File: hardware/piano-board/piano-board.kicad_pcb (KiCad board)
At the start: 2 copper layers, 100 x 60 mm, 29 parts, among them J1 AVR-ISP-6, Q1 Q_NMOS_GSD, Q2 Q_PMOS_GSD, SW1 SW_SPDT, U1 ATmega328PB-A

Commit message: Improve CR2032 holder footprint
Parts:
- moved BT1 3.05 mm to (238.2, 51.8), turned to -45 degrees
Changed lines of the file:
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@@
 	(footprint "Thanassis_Foot:MP000360"
 		(layer "F.Cu")
-		(at 236.5 49.25)
+		(at 238.25 51.75 -45)
 		(property "Reference" "BT1"
-			(at 0 3.75 0)
+			(at 0 3.749999 -45)
 			(unlocked yes)
 			(layer "F.SilkS")
@@
 		)
 		(property "Value" "Battery_Cell"
-			(at 0 1 0)
+			(at 0 1 -45)
 			(unlocked yes)
 			(layer "F.Fab")
@@
 		)
 		(property "Footprint" "Thanassis_Foot:MP000360"
-			(at 0 0 0)
+			(at 0 0 -45)
 			(unlocked yes)
 			(layer "F.Fab")
@@
 		)
 		(property "Datasheet" ""
-			(at 0 0 0)
+			(at 0 0 -45)
 			(unlocked yes)
 			(layer "F.Fab")
@@
 		)
 		(property "Description" "Single-cell battery"
-			(at 0 0 0)
+			(at 0 0 -45)
 			(unlocked yes)
 			(layer "F.Fab")
@@
 		(attr through_hole)
 		(fp_line
-			(start -10.6 -5)
-			(end -10.6 5)
-			(stroke
-				(width 0.12)
-				(type default)
-			)
-			(layer "F.SilkS")
-		)
-		(fp_line
 			(start -10.6 5)
 			(end -3.9 10.25)
@@
 		)
 		(fp_line
+			(start -10.6 5)
+			(end -10.6 2.5)
+			(stroke
+				(width 0.12)
+				(type default)
+			)
+			(layer "F.SilkS")
+		)
+		(fp_line
 			(start -3.9 10.25)
 			(end 3.9 10.25)
@@
 		)
 		(fp_line
+			(start -10.6 -5)
+			(end -10.6 -2.5)
+			(stroke
+				(width 0.12)
+				(type default)
+			)
+			(layer "F.SilkS")
+		)
+		(fp_line
+			(start -6.51 -7.99)
+			(end -10.6 -5)
+			(stroke
+				(width 0.12)
+				(type default)
+			)
+			(layer "F.SilkS")
+		)
+		(fp_line
+			(start -6.51 -7.99)
+			(end -4 -7.99)
+			(stroke
+				(width 0.12)
+				(type default)
+			)
+			(layer "F.SilkS")
+		)
+		(fp_line
+			(start 10.6 2.5)
+			(end 10.6 5)
+			(stroke
+				(width 0.12)
+				(type default)
+			)
+			(layer "F.SilkS")
+		)
+		(fp_line
+			(start 4 -7.99)
+			(end 6.51 -7.99)
+			(stroke
+				(width 0.12)
+				(type default)
+			)
+			(layer "F.SilkS")
+		)
+		(fp_line
+			(start 6.51 -7.99)
+			(end 10.6 -5)
+			(stroke
+				(width 0.12)
+				(type default)
+			)
+			(layer "F.SilkS")
+		)
+		(fp_line
 			(start 10.6 -5)
-			(end 10.6 5)
-			(stroke
-				(width 0.12)
-				(type default)
-			)
-			(layer "F.SilkS")
-		)
-		(fp_line
-			(start -10.6 -7.99)
-			(end 10.6 -7.99)
-			(stroke
-				(width 0.12)
-				(type default)
-			)
+			(end 10.6 -2.5)
+			(stroke
+				(width 0.12)
+				(type default)
+			)
+			(layer "F.SilkS")
+		)
+		(fp_arc
+			(start 4 -7.99)
+			(mid 0 -6.737326)
+			(end -4 -7.99)
+			(stroke
+				(width 0.12)
+				(type default)
+			)
+			(layer "F.SilkS")
+		)
+		(fp_circle
+			(center 0 0)
+			(end 10 0)
+			(stroke
+				(width 0.12)
+				(type dash)
+			)
+			(fill none)
 			(layer "Dwgs.User")
-		)
-		(fp_line
-			(start -13 -8.5)
-			(end -13 5)
-			(stroke
-				(width 0.05)
-				(type default)
-			)
-			(layer "F.CrtYd")
 		)
 		(fp_line
@@
 		)
 		(fp_line
+			(start -13 -5)
+			(end -13 5)
+			(stroke
+				(width 0.05)
+				(type default)
+			)
+			(layer "F.CrtYd")
+		)
+		(fp_line
 			(start 4.000001 11)
 			(end 13 5)
@@
 		)
 		(fp_line
-			(start 13 -8.5)
-			(end -13 -8.5)
+			(start -5.5 -10.5)
+			(end -13 -5)
 			(stroke
 				(width 0.05)
@@
 		(fp_line
 			(start 13 5)
-			(end 13 -8.5)
+			(end 13 -5)
+			(stroke
+				(width 0.05)
+				(type default)
+			)
+			(layer "F.CrtYd")
+		)
+		(fp_line
+			(start 5.5 -10.5)
+			(end -5.5 -10.5)
+			(stroke
+				(width 0.05)
+				(type default)
+			)
+			(layer "F.CrtYd")
+		)
+		(fp_line
+			(start 13 -5)
+			(end 5.5 -10.5)
 			(stroke
 				(width 0.05)
@@
 		)
 		(fp_text user "+"
-			(at 0 7.5 0)
+			(at 0 7.5 -45)
 			(unlocked yes)
 			(layer "F.SilkS")
@@
 		)
 		(fp_text user "${REFERENCE}"
-			(at 2.75 4.75 0)
+			(at 2.75 4.75 -45)
 			(unlocked yes)
 			(layer "F.Fab")
@@
 		)
 		(pad "1" thru_hole circle
-			(at -10.6 0 45)
+			(at -10.6 0)
 			(size 4 4)
 			(drill 2)
@@
 		)
 		(pad "1" thru_hole circle
-			(at 10.6 0 45)
+			(at 10.6 0)
 			(size 4 4)
 			(drill 2)
@@
 		)
 		(pad "2" smd rect
-			(at 0 0)
+			(at 0 0 315)
 			(size 4 4)
 			(layers "F.Cu" "F.Paste" "F.Mask")
@@
 		)
 		(layer "Dwgs.User")
+	)
+	(gr_line
+		(start 250 40)
+		(end 227.5 62.5)
+		(stroke
+			(width 0.1)
+			(type default)
+		)
+		(layer "Dwgs.User")

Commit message: Route key connections
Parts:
- added SW2: OCT_INC, Thanassis_Foot:SW_PUSH_ADAFRUIT_SMALL, F.Cu at (216.7, 48.5)
- added SW3: OCT_DWN, Thanassis_Foot:SW_PUSH_ADAFRUIT_SMALL, F.Cu at (216.7, 54.5)
- added SW4: WAVE_CHANGE, Thanassis_Foot:SW_PUSH_ADAFRUIT_SMALL, F.Cu at (174.5, 56.0)
- moved C1 23.0 mm to (193.5, 48.5), turned to 90 degrees
- moved C4 19.7 mm to (195.3, 48.5), turned to -90 degrees
- moved FB1 19.3 mm to (210.0, 41.5)
- moved C2 15.9 mm to (210.0, 43.5)
- moved C5 12.9 mm to (171.3, 44.2)
- moved C6 12.8 mm to (175.0, 44.2)
- moved R12 10.3 mm to (209.0, 54.5), turned to -45 degrees
- moved C3 10.1 mm to (207.7, 49.2), turned to 90 degrees
- moved R11 8.78 mm to (207.5, 56.0), turned to -45 degrees
- moved R1 7.55 mm to (186.5, 59.0)
- moved R2 7.55 mm to (188.5, 59.0)
- moved R3 7.55 mm to (190.5, 59.0)
- moved R4 7.55 mm to (192.5, 59.0)
- moved R5 7.55 mm to (194.5, 59.0)
- moved R6 7.55 mm to (196.5, 59.0)
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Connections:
- net /KEY_0_PAD renamed KEY_0_PAD
- net /KEY_10_PAD renamed KEY_10_PAD
- net /KEY_11_PAD renamed KEY_11_PAD
- net /KEY_1_PAD renamed KEY_1_PAD
- net /KEY_2_PAD renamed KEY_2_PAD
- net /KEY_3_PAD renamed KEY_3_PAD
- net /KEY_4_PAD renamed KEY_4_PAD
- net /KEY_5_PAD renamed KEY_5_PAD
- net /KEY_6_PAD renamed KEY_6_PAD
- net /KEY_7_PAD renamed KEY_7_PAD
- net /KEY_8_PAD renamed KEY_8_PAD
- net /KEY_9_PAD renamed KEY_9_PAD
- U1 pad 1: KEY_11 -> KEY_7
- U1 pad 10: unconnected-(U1-PD6-Pad10) -> OCT_DEC
- U1 pad 11: unconnected-(U1-PD7-Pad11) -> WAVE_CHANGE
- U1 pad 12: MCU_AUDIO -> unconnected-(U1-PB0-Pad12)
- U1 pad 19: KEY_9 -> unconnected-(U1-PE2-Pad19)
- U1 pad 2: unconnected-(U1-PD4-Pad2) -> KEY_8
- U1 pad 22: KEY_10 -> MCU_AUDIO
- U1 pad 3: KEY_7 -> KEY_9
- U1 pad 6: KEY_8 -> unconnected-(U1-PE1-Pad6)
- U1 pad 7: unconnected-(U1-XTAL1/PB6-Pad7) -> KEY_10
- U1 pad 8: unconnected-(U1-XTAL2/PB7-Pad8) -> KEY_11
- U1 pad 9: unconnected-(U1-PD5-Pad9) -> OCT_INC
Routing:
- net KEY_11_PAD: track 0.00 -> 57.4 mm
- net KEY_0_PAD: track 0.00 -> 51.8 mm, vias 0 -> 2
- net KEY_9_PAD: track 0.00 -> 46.0 mm, vias 0 -> 2
- net KEY_2_PAD: track 0.00 -> 41.5 mm, vias 0 -> 1
- net KEY_7_PAD: track 0.00 -> 36.5 mm, vias 0 -> 2
- net KEY_10_PAD: track 0.00 -> 32.2 mm
- net KEY_4_PAD: track 0.00 -> 26.0 mm
- net KEY_1_PAD: track 0.00 -> 25.4 mm
- net KEY_5_PAD: track 0.00 -> 23.1 mm
- net KEY_8_PAD: track 0.00 -> 18.0 mm
- net KEY_3_PAD: track 0.00 -> 12.1 mm
- net KEY_6_PAD: track 0.00 -> 8.01 mm
- net GND: vias 0 -> 83
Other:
- board text added: "BUZZER"
- board text added: "OCT"
- board text added: "PCB Touch Piano v1.0"
- board text added: "RST"
- board text added: "R[1..12]"
- board text added: "Thanassis Frank 11/24"
- board text added: "WAVE"

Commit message: Re-assign key pins on MCU
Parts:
- moved C1 3.35 mm to (190.5, 50.0)
- moved C4 3.35 mm to (192.3, 50.0)
- moved U1 3.35 mm to (198.5, 50.5)
- moved C3 2.81 mm to (205.0, 50.0)
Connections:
- U1 pad 1: KEY_7 -> KEY_9
- U1 pad 2: KEY_8 -> KEY_10
- U1 pad 27: unconnected-(U1-PC4-Pad27) -> KEY_4
- U1 pad 28: unconnected-(U1-PC5-Pad28) -> KEY_5
- U1 pad 3: KEY_9 -> KEY_11
- U1 pad 30: KEY_4 -> KEY_6
- U1 pad 31: KEY_5 -> KEY_7
- U1 pad 32: KEY_6 -> KEY_8
- U1 pad 7: KEY_10 -> unconnected-(U1-XTAL1/PB6-Pad7)
- U1 pad 8: KEY_11 -> unconnected-(U1-XTAL2/PB7-Pad8)
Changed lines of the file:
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@@
 	(net 36 "unconnected-(SW1-C-Pad3)")
 	(net 37 "unconnected-(U1-PB2-Pad14)")
-	(net 38 "unconnected-(U1-PC5-Pad28)")
-	(net 39 "unconnected-(U1-PC4-Pad27)")
+	(net 38 "unconnected-(U1-XTAL1{slash}PB6-Pad7)")
+	(net 39 "unconnected-(U1-XTAL2{slash}PB7-Pad8)")
 	(net 40 "unconnected-(U1-PB1-Pad13)")
 	(net 41 "/BAT+")
@@
 	(footprint "Package_QFP:TQFP-32_7x7mm_P0.8mm"
 		(layer "F.Cu")
-		(at 201.5 49 180)
+		(at 198.5 50.5 180)
 		(descr "32-Lead Plastic Thin Quad Flatpack (PT) - 7x7x1.0 mm Body, 2.00 mm [TQFP] (see Microchip Packaging Specification 00000049BS.pdf)")
 		(tags "QFP 0.8")
@@
 			(size 1.6 0.55)
 			(layers "F.Cu" "F.Paste" "F.Mask")
-			(net 27 "KEY_7")
+			(net 30 "KEY_9")
 			(pinfunction "PD3")
 			(pintype "bidirectional")
@@
 			(size 1.6 0.55)
 			(layers "F.Cu" "F.Paste" "F.Mask")
-			(net 29 "KEY_8")
+			(net 32 "KEY_10")
 			(pinfunction "PD4")
 			(pintype "bidirectional")
@@
 			(size 1.6 0.55)
 			(layers "F.Cu" "F.Paste" "F.Mask")
-			(net 30 "KEY_9")
+			(net 34 "KEY_11")
 			(pinfunction "PE0")
 			(pintype "bidirectional")
@@
 			(size 1.6 0.55)
 			(layers "F.Cu" "F.Paste" "F.Mask")
-			(net 32 "KEY_10")
+			(net 38 "unconnected-(U1-XTAL1{slash}PB6-Pad7)")
 			(pinfunction "XTAL1/PB6")
-			(pintype "bidirectional")
+			(pintype "bidirectional+no_connect")
 		)
 		(pad "8" smd rect
@@
 			(size 1.6 0.55)
 			(layers "F.Cu" "F.Paste" "F.Mask")
-			(net 34 "KEY_11")
+			(net 39 "unconnected-(U1-XTAL2{slash}PB7-Pad8)")
 			(pinfunction "XTAL2/PB7")
-			(pintype "bidirectional")
+			(pintype "bidirectional+no_connect")
 		)
 		(pad "9" smd rect
@@
 			(size 1.6 0.55)
 			(layers "F.Cu" "F.Paste" "F.Mask")
-			(net 39 "unconnected-(U1-PC4-Pad27)")
+			(net 20 "KEY_4")
 			(pinfunction "PC4")
-			(pintype "bidirectional+no_connect")
+			(pintype "bidirectional")
 		)
 		(pad "28" smd rect
@@
 			(size 1.6 0.55)
 			(layers "F.Cu" "F.Paste" "F.Mask")
-			(net 38 "unconnected-(U1-PC5-Pad28)")
+			(net 22 "KEY_5")
 			(pinfunction "PC5")
-			(pintype "bidirectional+no_connect")
+			(pintype "bidirectional")
 		)
 		(pad "29" smd rect
@@
 			(size 1.6 0.55)
 			(layers "F.Cu" "F.Paste" "F.Mask")
-			(net 20 "KEY_4")
+			(net 25 "KEY_6")
 			(pinfunction "PD0")
 			(pintype "bidirectional")
@@
 			(size 1.6 0.55)
 			(layers "F.Cu" "F.Paste" "F.Mask")
-			(net 22 "KEY_5")
+			(net 27 "KEY_7")
 			(pinfunction "PD1")
 			(pintype "bidirectional")
@@
 			(size 1.6 0.55)
 			(layers "F.Cu" "F.Paste" "F.Mask")
-			(net 25 "KEY_6")
+			(net 29 "KEY_8")
 			(pinfunction "PD2")
 			(pintype "bidirectional")
@@
 	(footprint "Capacitor_SMD:C_0603_1608Metric_Pad1.08x0.95mm_HandSolder"
 		(layer "F.Cu")
-		(at 195.312815 48.46967 -90)
+		(at 192.312815 49.96967 -90)
 		(descr "Capacitor SMD 0603 (1608 Metric), square (rectangular) end terminal, IPC_7351 nominal with elongated pad for handsoldering. (Body size source: IPC-SM-782 page 76, https://www.pcb-3d.com/wordpress/wp-content/uploads/ipc-sm-782a_amendment_1_and_2.pdf), generated with kicad-footprint-generator")
 		(tags "capacitor handsolder")
@@
 	(footprint "Capacitor_SMD:C_0603_1608Metric_Pad1.08x0.95mm_HandSolder"
 		(layer "F.Cu")
-		(at 207.687184 49.176777 90)
+		(at 205 50 90)
 		(descr "Capacitor SMD 0603 (1608 Metric), square (rectangular) end terminal, IPC_7351 nominal with elongated pad for handsoldering. (Body size source: IPC-SM-782 page 76, https://www.pcb-3d.com/wordpress/wp-content/uploads/ipc-sm-782a_amendment_1_and_2.pdf), generated with kicad-footprint-generator")
 		(tags "capacitor handsolder")
@@
 	(footprint "Capacitor_SMD:C_0603_1608Metric_Pad1.08x0.95mm_HandSolder"
 		(layer "F.Cu")
-		(at 193.545048 48.46967 90)
+		(at 190.545048 49.96967 90)
 		(descr "Capacitor SMD 0603 (1608 Metric), square (rectangular) end terminal, IPC_7351 nominal with elongated pad for handsoldering. (Body size source: IPC-SM-782 page 76, https://www.pcb-3d.com/wordpress/wp-content/uploads/ipc-sm-782a_amendment_1_and_2.pdf), generated with kicad-footprint-generator")
 		(tags "capacitor handsolder")
@@
 		(polygon
 			(pts
-				(xy 188.5 63) (xy 188.5 80) (xy 198.5 80) (xy 198.5 62.5) (xy 250 62.5) (xy 250 100) (xy 150 100)
+				(xy 187.5 63) (xy 187.5 80) (xy 198.5 80) (xy 198.5 62.5) (xy 250 62.5) (xy 250 100) (xy 150 100)
 				(xy 150 62.5)
 			)

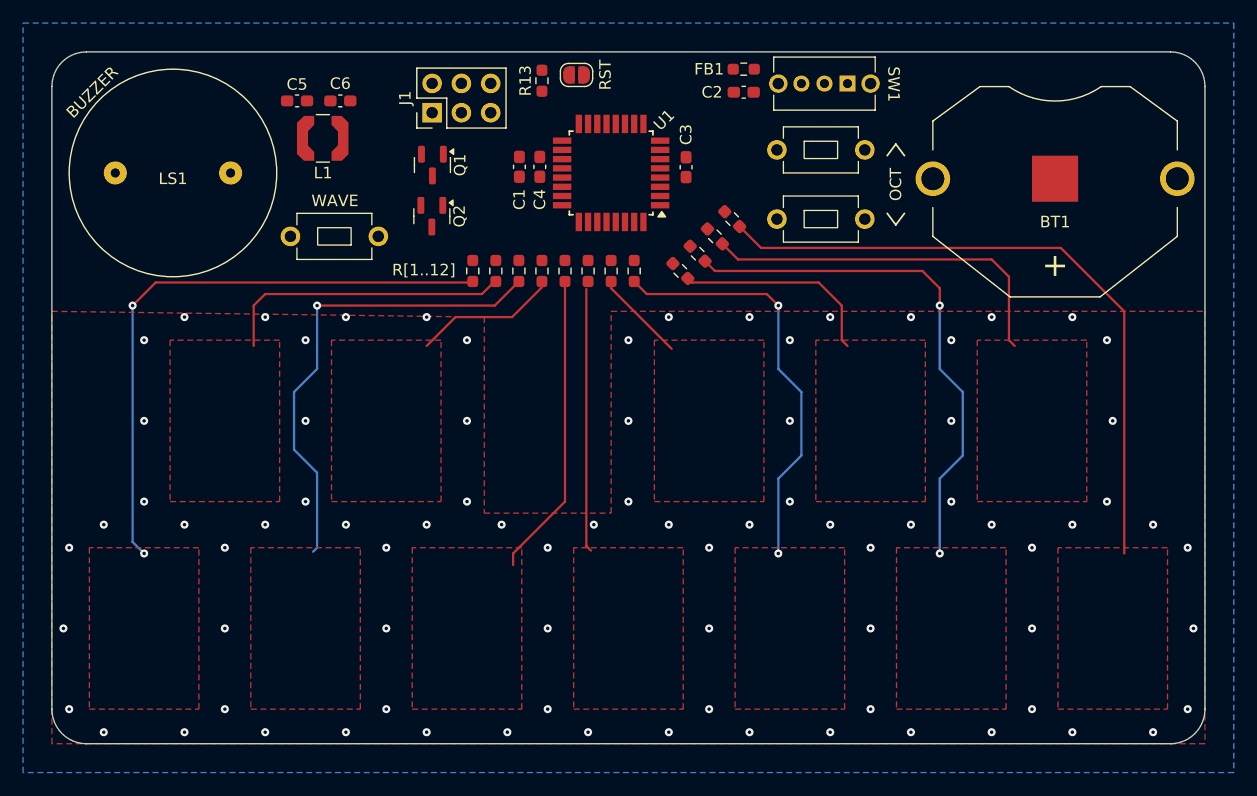
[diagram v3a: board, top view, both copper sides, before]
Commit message: Route all signals
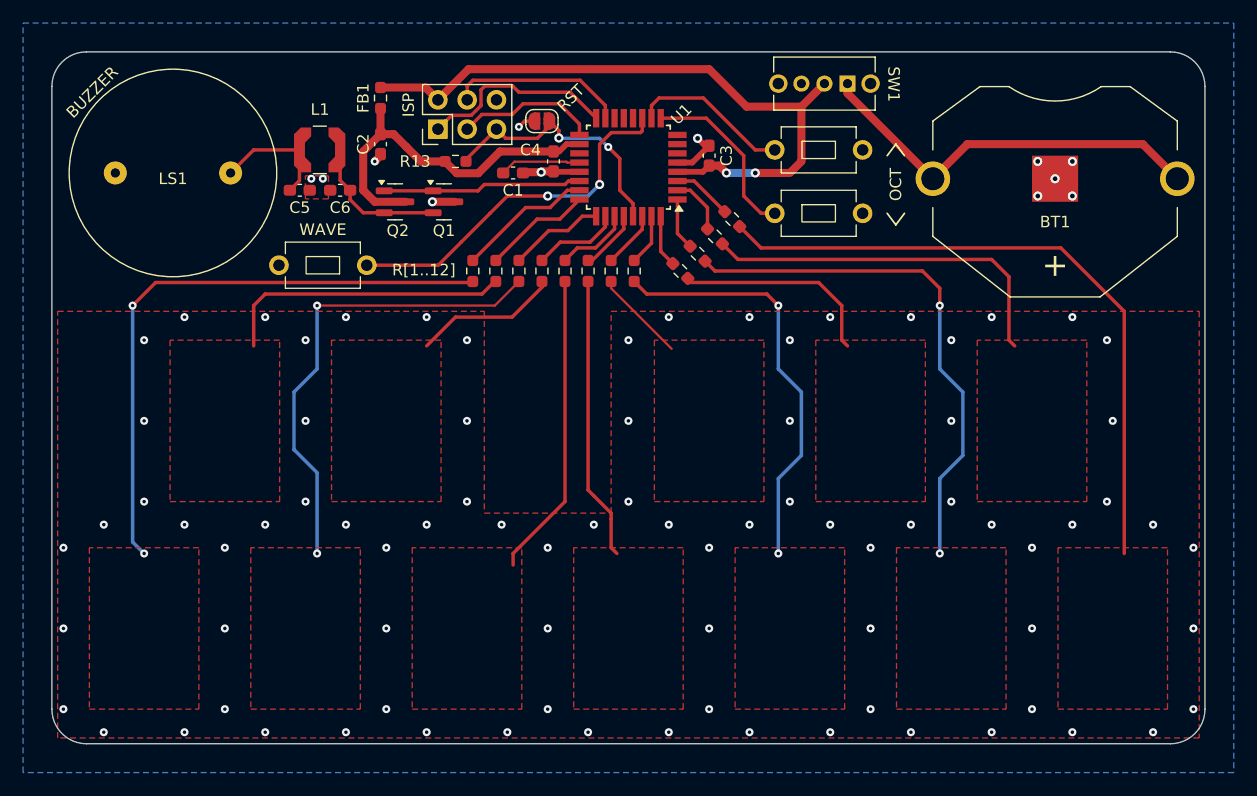
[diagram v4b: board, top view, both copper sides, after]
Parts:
- moved C2 31.8 mm to (178.5, 48.0), turned to -90 degrees
- moved FB1 31.6 mm to (178.5, 44.0), turned to -90 degrees
- moved R13 10.3 mm to (185.0, 49.5), turned to 0 degrees
- moved C5 7.75 mm to (171.5, 52.0)
- moved C6 7.75 mm to (175.0, 52.0)
- moved JP1 5.00 mm to (192.5, 46.0), turned to 0 degrees
- moved Q2 3.43 mm to (179.8, 53.0), turned to 0 degrees
- moved Q1 3.34 mm to (184.0, 53.0), turned to 0 degrees
- moved SW4 2.69 mm to (173.5, 58.5)
- moved C3 2.24 mm to (207.0, 49.0)
- moved U1 1.58 mm to (200.0, 50.0)
- moved J1 1.51 mm to (183.5, 46.7)
- moved C4 1.28 mm to (193.5, 49.5)
- moved L1 1.03 mm to (173.2, 48.5)
- moved C1 0.76 mm to (190.0, 50.5), turned to 180 degrees
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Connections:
- R13 pad 1: VCC -> AVCC
- U1 pad 10: OCT_DEC -> OCT_INC
- U1 pad 9: OCT_INC -> OCT_DEC
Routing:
- net VCC: track 0.00 -> 58.7 mm, vias 0 -> 2
- net /BAT+: track 0.00 -> 35.0 mm
- net WAVE_CHANGE: track 0.00 -> 31.9 mm, vias 0 -> 2
- net AVCC: track 0.00 -> 30.5 mm
- net RST_DBG_PIN: track 0.00 -> 23.0 mm, vias 0 -> 2
- net MCU_AUDIO: track 0.00 -> 17.3 mm
- net MISO_0: track 0.00 -> 17.2 mm
- net MOSI_0: track 0.00 -> 15.4 mm
- net OCT_DEC: track 0.00 -> 15.4 mm
- net AUDIO_AMP_OUT: track 0.00 -> 14.9 mm
- net OCT_INC: track 0.00 -> 13.9 mm
- net GND: track 0.00 -> 13.4 mm, vias 83 -> 95
- net SCK_0: track 0.00 -> 12.3 mm
- net KEY_0: track 0.00 -> 11.8 mm
- net AUDIO_FLTR_OUT: track 0.00 -> 11.7 mm
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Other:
- board text added: "ISP"

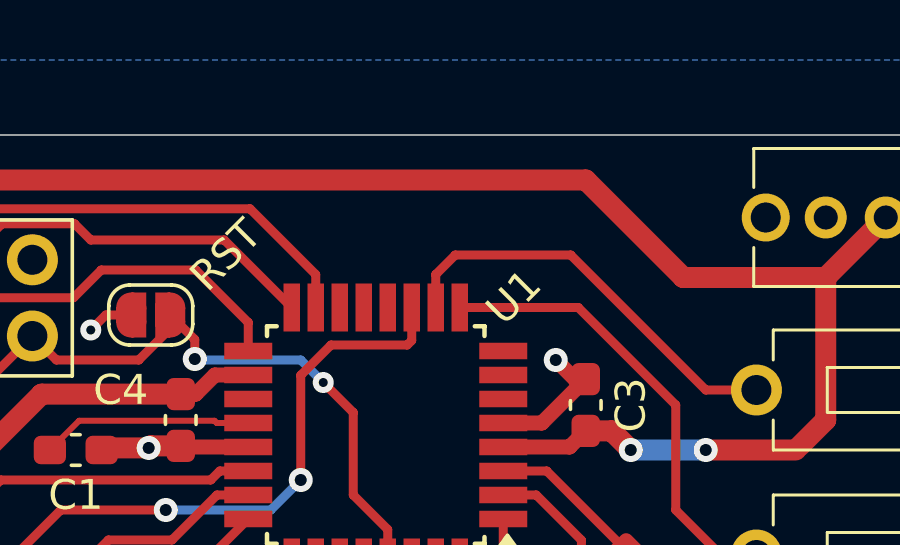
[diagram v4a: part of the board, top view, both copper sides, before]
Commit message: Add status LED
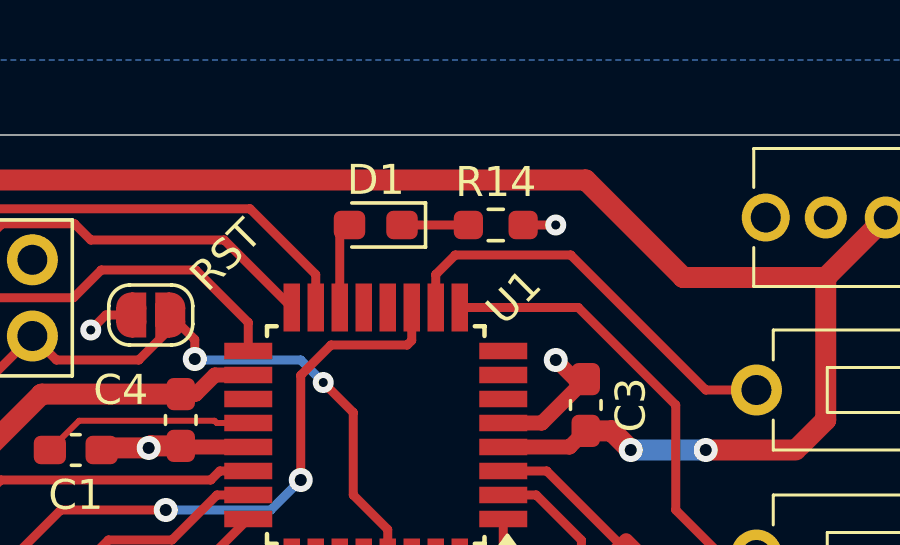
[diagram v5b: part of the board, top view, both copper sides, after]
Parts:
- added D1: LED, LED_SMD:LED_0603_1608Metric_Pad1.05x0.95mm_HandSolder, F.Cu at (200.0, 43.0)
- added R14: R, Resistor_SMD:R_0603_1608Metric_Pad0.98x0.95mm_HandSolder, F.Cu at (204.0, 43.0)
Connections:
- U1 pad 14: unconnected-(U1-PB2-Pad14) -> /STATUS_LED
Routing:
- net /STATUS_LED: track 0.00 -> 2.88 mm
- net Net-(D1-K): track 0.00 -> 2.21 mm
- net GND: track 13.4 -> 14.5 mm, vias 95 -> 96
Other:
- board text added: "Keys are about 2pF vs max of 32pF"

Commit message: Polish for manufacturing
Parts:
- added R15: 0, Resistor_SMD:R_0603_1608Metric_Pad0.98x0.95mm_HandSolder, F.Cu at (173.5, 45.0)
- moved Q1 4.85 mm to (179.3, 54.0), turned to 180 degrees
- moved Q2 3.87 mm to (183.5, 54.0), turned to 180 degrees
- moved SW2 0.50 mm to (217.0, 48.5)
- moved SW3 0.50 mm to (217.0, 54.0)
- moved L1 0.26 mm to (173.5, 48.5)
- turned LS1 to -135 degrees
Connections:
- LS1 pad 1: AUDIO_FLTR_OUT -> Net-(LS1-Pad1)
- Q1 pad 2: AUDIO_AMP_OUT -> GND
- Q1 pad 3: GND -> AUDIO_AMP_OUT
- Q2 pad 2: AUDIO_AMP_OUT -> AVCC
- Q2 pad 3: AVCC -> AUDIO_AMP_OUT
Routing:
- net GND: track 14.5 -> 31.9 mm, vias 96 -> 97
- net Net-(LS1-Pad1): track 0.00 -> 9.37 mm
- net AVCC: track 30.5 -> 23.7 mm
- net AUDIO_AMP_OUT: track 14.9 -> 11.9 mm
- net KEY_11_PAD: track 57.4 -> 60.2 mm
- net KEY_0_PAD: track 52.3 -> 54.2 mm, vias 2 -> 0
- net KEY_10_PAD: track 32.2 -> 30.8 mm
- net AUDIO_FLTR_OUT: track 11.7 -> 10.7 mm
- net KEY_9_PAD: track 46.0 -> 45.1 mm
- net MCU_AUDIO: track 17.3 -> 17.9 mm
- net /BAT+: track 35.0 -> 35.6 mm
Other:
- board text added: "OFF"
- board text added: "ON"
- board text added: "Thanassis Frank 12/24"
- board text added: "WayWayWay"
- board text removed: "Thanassis Frank 11/24"
